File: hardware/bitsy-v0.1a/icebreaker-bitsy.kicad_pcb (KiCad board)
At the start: 4 copper layers, 38.1 x 17.8 mm, 95 parts, among them J1 Conn_01x01, J10 Conn_01x01, J11 Conn_01x01, J12 Conn_01x01, J13 Conn_01x01, J14 Jumper, J15 Jumper, J16 Jumper, J17 Jumper, J18 Jumper, J19 Jumper, J2 Conn_01x01, J20 Conn_01x01, J21 Conn_01x01, J22 Conn_01x01, J23 Conn_01x01, J24 Conn_01x01, J25 Conn_01x01, J26 Conn_01x01, J27 Conn_01x01, J28 Conn_01x01, J29 Conn_01x01, J3 Conn_01x01, J30 Conn_01x01, J31 Conn_01x01, J32 Conn_01x01, J33 Conn_01x01, J34 Conn_01x01, J35 Conn_01x01, J36 Conn_01x01, J37 Conn_01x01, J38 Jumper, J4 Conn_01x01, J41 Conn_01x01, J42 Conn_01x01, J43 Conn_01x01, J44 Conn_01x01, J45 Conn_01x01, J46 Conn_01x01, J47 Conn_01x01, J48 Conn_01x01, J49 Conn_01x01, J5 Conn_01x01, J6 Conn_01x01, J7 Conn_01x01, J8 Conn_01x01, J9 Conn_01x01, P1 USB_OTG, SW1 TACT, U1 USBLC6-2, U2 3.3V, U3 1V2, U5 W25Q, U6 ICE5LP4K-SG48, X1 12MHz

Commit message: Added pinout information and updated schematic.
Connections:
- net /IOT_36b renamed /IOT_36B
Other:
- board text added: "+3.3V xx 15"
- board text added: "16 xx GND"
- board text added: "17 25 IOT_36B"
- board text added: "18 26 IOT_39A"
- board text added: "19 27 IOT_38B"
- board text added: "20 28 IOT_41A"
- board text added: "21 31 IOT_42B"
- board text added: "22 32 IOT_43A"
- board text added: "23 34 IOT_44B"
- board text added: "24 36 IOT_48B"
- board text added: "25 39 ~LED_RED"
- board text added: "26 40 ~LED_GRN"
- board text added: "27 41 ~LED_BLU"
- board text added: "28 xx +1.2V"
- board text added: "29 xx +3.3V"
- board text added: "30 xx +5V"
- board text added: "36 20 IOB_25B_G3"
- board text added: "37 xx SCK"
- board text added: "38 21 IOB_23B"
- board text added: "39 xx SS_B/CS"
- board text added: "40 23 IOT_37A"
- board text added: "CDONE xx 33"
- board text added: "CRESET xx 35"
- board text added: "FLASH_MISO/IO1 xx 14"
- board text added: "FLASH_MOSI/IO0 xx 31"
- board text added: "GND xx 01"
- board text added: "IOB_0A 46 04"
- board text added: "IOB_13B 06 10"
- board text added: "IOB_16A 09 11"
- board text added: "IOB_22A FLASH_~WP~/IO2 12 13"
- board text added: "IOB_24A FLASH_~HLD~/~RST~/IO3 13 12"
- board text added: "IOB_29B 19 34"
- board text added: "IOB_2A 47 05"
- board text added: "IOB_31B 18 32"
- board text added: "IOB_3B_G6 44 02"
- board text added: "IOB_4A 48 06"
- board text added: "IOB_5B 45 03"
- board text added: "IOB_6A 02 07"
- board text added: "IOB_8A 04 09"
- board text added: "IOB_9B 03 08"

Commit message: Fixed pin header 3d models.
We had some of the models doubled up or not fully disabled. Now the TH
pin headers are all using KiCad V5 3d model locations and are all
disabled.

This fixes #23
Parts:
- removed REF**: 1b2_Logo_SilkS_5mm, pkl_logos:1b2_Logo_SilkS_5mm
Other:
- board text removed: "1Bitsquared (C) 2018"

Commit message: Added more legend silkscreen to ears.
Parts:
- added REF**: 1b2_Logo_SilkS_5mm, pkl_logos:1b2_Logo_SilkS_5mm, B.Cu at (41.6, 47.4)
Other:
- board text added: "1Bitsquared (C) 2018"
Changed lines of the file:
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@@
   (general
     (thickness 1.6)
-    (drawings 160)
+    (drawings 161)
     (tracks 669)
     (zones 0)
-    (modules 94)
+    (modules 95)
     (nets 60)
   )
@@
     (add_net "Net-(P1-Pad4)")
     (add_net "Net-(R7-Pad2)")
+  )
+  (module pkl_logos:1b2_Logo_SilkS_5mm locked (layer B.Cu)
+    (at 41.628314 47.429988 90)
+    (fp_text reference REF** (at 0 -4 90) (layer B.Fab) hide
+      (effects (font (size 1 1) (thickness 0.15)) (justify mirror))
+    )
+    (fp_text value 1b2_Logo_SilkS_5mm (at 0 4 90) (layer B.Fab) hide
+      (effects (font (size 1 1) (thickness 0.15)) (justify mirror))
+    )
+    (fp_line (start -0.5 0.5) (end -0.5 2.5) (layer B.SilkS) (width 0.2))
+    (fp_line (start -0.5 2.5) (end -2.5 2.5) (layer B.SilkS) (width 0.2))
+    (fp_line (start -2.5 2.5) (end -2.5 0.5) (layer B.SilkS) (width 0.2))
+    (fp_line (start -2.5 0.5) (end -0.5 0.5) (layer B.SilkS) (width 0.2))
+    (fp_line (start -0.5 2.5) (end 0 2) (layer B.SilkS) (width 0.2))
+    (fp_line (start 0 2) (end 0 0) (layer B.SilkS) (width 0.2))
+    (fp_line (start 0 0) (end -0.5 0.5) (layer B.SilkS) (width 0.2))
+    (fp_line (start -2.5 0.5) (end -2 0) (layer B.SilkS) (width 0.2))
+    (fp_line (start -2 0) (end 0 0) (layer B.SilkS) (width 0.2))
+    (fp_line (start 2 2) (end 0.5 2) (layer B.SilkS) (width 0.2))
+    (fp_line (start 0.5 2) (end 0.5 -0.5) (layer B.SilkS) (width 0.2))
+    (fp_line (start 0.5 -0.5) (end -2 -0.5) (layer B.SilkS) (width 0.2))
+    (fp_line (start -2 -0.5) (end -2 -2) (layer B.SilkS) (width 0.2))
+    (fp_line (start -2 -2) (end 2 -2) (layer B.SilkS) (width 0.2))
+    (fp_line (start 2 -2) (end 2 2) (layer B.SilkS) (width 0.2))
+    (fp_line (start 2 2) (end 2.5 1.5) (layer B.SilkS) (width 0.2))
+    (fp_line (start 2.5 1.5) (end 2.5 -2.5) (layer B.SilkS) (width 0.2))
+    (fp_line (start 2.5 -2.5) (end 2 -2) (layer B.SilkS) (width 0.2))
+    (fp_line (start -2 -2) (end -1.5 -2.5) (layer B.SilkS) (width 0.2))
+    (fp_line (start -1.5 -2.5) (end 2.5 -2.5) (layer B.SilkS) (width 0.2))
   )
   (module pkl_jumpers:J_0603 (layer B.Cu)
@@
       (net 2 +3V3))
   )
+  (gr_text "1Bitsquared\n(C) 2018" (at 37.4 47.3 270) (layer B.SilkS)
+    (effects (font (size 1 1) (thickness 0.25)) (justify mirror))
+  )
   (gr_line (start 79.2 38.6) (end 79.2 47.5) (layer Cmts.User) (width 0.2))

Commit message: Replaced/added the null logo to the boards.
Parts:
- REF**: value 1b2_Logo_SilkS_5mm -> null_Logo_SilkS_5mm; footprint pkl_logos:1b2_Logo_SilkS_5mm -> pkl_logos:null_Logo_SilkS_5mm
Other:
- board text added: "NULL"
- board text removed: "1Bitsquared (C) 2018"
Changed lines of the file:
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@@
-(kicad_pcb (version 20171130) (host pcbnew 5.1.2-f72e74a~84~ubuntu18.04.1)
+(kicad_pcb (version 20171130) (host pcbnew 5.1.5-52549c5~86~ubuntu19.10.1)
   (general
     (thickness 1.6)
@@
     (add_net "Net-(R7-Pad2)")
   )
-  (module pkl_logos:1b2_Logo_SilkS_5mm locked (layer B.Cu)
+  (module pkl_logos:null_Logo_SilkS_5mm locked (layer B.Cu)
     (at 41.628314 47.429988 90)
     (fp_text reference REF** (at 0 -4 90) (layer B.Fab) hide
       (effects (font (size 1 1) (thickness 0.15)) (justify mirror))
     )
-    (fp_text value 1b2_Logo_SilkS_5mm (at 0 4 90) (layer B.Fab) hide
+    (fp_text value null_Logo_SilkS_5mm (at 0 4 90) (layer B.Fab) hide
       (effects (font (size 1 1) (thickness 0.15)) (justify mirror))
     )
-    (fp_line (start -0.5 0.5) (end -0.5 2.5) (layer B.SilkS) (width 0.2))
-    (fp_line (start -0.5 2.5) (end -2.5 2.5) (layer B.SilkS) (width 0.2))
-    (fp_line (start -2.5 2.5) (end -2.5 0.5) (layer B.SilkS) (width 0.2))
-    (fp_line (start -2.5 0.5) (end -0.5 0.5) (layer B.SilkS) (width 0.2))
-    (fp_line (start -0.5 2.5) (end 0 2) (layer B.SilkS) (width 0.2))
-    (fp_line (start 0 2) (end 0 0) (layer B.SilkS) (width 0.2))
-    (fp_line (start 0 0) (end -0.5 0.5) (layer B.SilkS) (width 0.2))
-    (fp_line (start -2.5 0.5) (end -2 0) (layer B.SilkS) (width 0.2))
-    (fp_line (start -2 0) (end 0 0) (layer B.SilkS) (width 0.2))
-    (fp_line (start 2 2) (end 0.5 2) (layer B.SilkS) (width 0.2))
-    (fp_line (start 0.5 2) (end 0.5 -0.5) (layer B.SilkS) (width 0.2))
-    (fp_line (start 0.5 -0.5) (end -2 -0.5) (layer B.SilkS) (width 0.2))
-    (fp_line (start -2 -0.5) (end -2 -2) (layer B.SilkS) (width 0.2))
-    (fp_line (start -2 -2) (end 2 -2) (layer B.SilkS) (width 0.2))
-    (fp_line (start 2 -2) (end 2 2) (layer B.SilkS) (width 0.2))
-    (fp_line (start 2 2) (end 2.5 1.5) (layer B.SilkS) (width 0.2))
-    (fp_line (start 2.5 1.5) (end 2.5 -2.5) (layer B.SilkS) (width 0.2))
-    (fp_line (start 2.5 -2.5) (end 2 -2) (layer B.SilkS) (width 0.2))
-    (fp_line (start -2 -2) (end -1.5 -2.5) (layer B.SilkS) (width 0.2))
-    (fp_line (start -1.5 -2.5) (end 2.5 -2.5) (layer B.SilkS) (width 0.2))
+    (fp_arc (start -0.4 -0.2) (end -0.7 -0.2) (angle 180) (layer B.SilkS) (width 0.15))
+    (fp_line (start 1 -0.5) (end 1.5 -0.5) (layer B.SilkS) (width 0.15))
+    (fp_line (start 1 0.5) (end 1 -0.5) (layer B.SilkS) (width 0.15))
+    (fp_line (start 0.2 -0.5) (end 0.7 -0.5) (layer B.SilkS) (width 0.15))
+    (fp_line (start 0.2 0.5) (end 0.2 -0.5) (layer B.SilkS) (width 0.15))
+    (fp_line (start -0.1 0.5) (end -0.1 -0.2) (layer B.SilkS) (width 0.15))
+    (fp_line (start -0.7 0.5) (end -0.7 -0.2) (layer B.SilkS) (width 0.15))
+    (fp_line (start -1 -0.5) (end -1 0.5) (layer B.SilkS) (width 0.15))
+    (fp_line (start -1.5 0.5) (end -1 -0.5) (layer B.SilkS) (width 0.15))
+    (fp_line (start -1.5 -0.5) (end -1.5 0.5) (layer B.SilkS) (width 0.15))
+    (fp_line (start 2.5 2.5) (end -2.5 2.5) (layer B.SilkS) (width 0.2))
+    (fp_line (start -2.5 2.5) (end -2.5 -2.5) (layer B.SilkS) (width 0.2))
+    (fp_line (start 2.5 2.5) (end 2.5 -2.5) (layer B.SilkS) (width 0.2))
+    (fp_line (start -2.5 -2.5) (end 2.5 -2.5) (layer B.SilkS) (width 0.2))
   )
   (module pkl_jumpers:J_0603 (layer B.Cu)
@@
       (net 2 +3V3))
   )
-  (gr_text "1Bitsquared\n(C) 2018" (at 37.4 47.3 270) (layer B.SilkS)
+  (gr_text NULL (at 37.4 47.3 270) (layer B.SilkS)
     (effects (font (size 1 1) (thickness 0.25)) (justify mirror))
   )

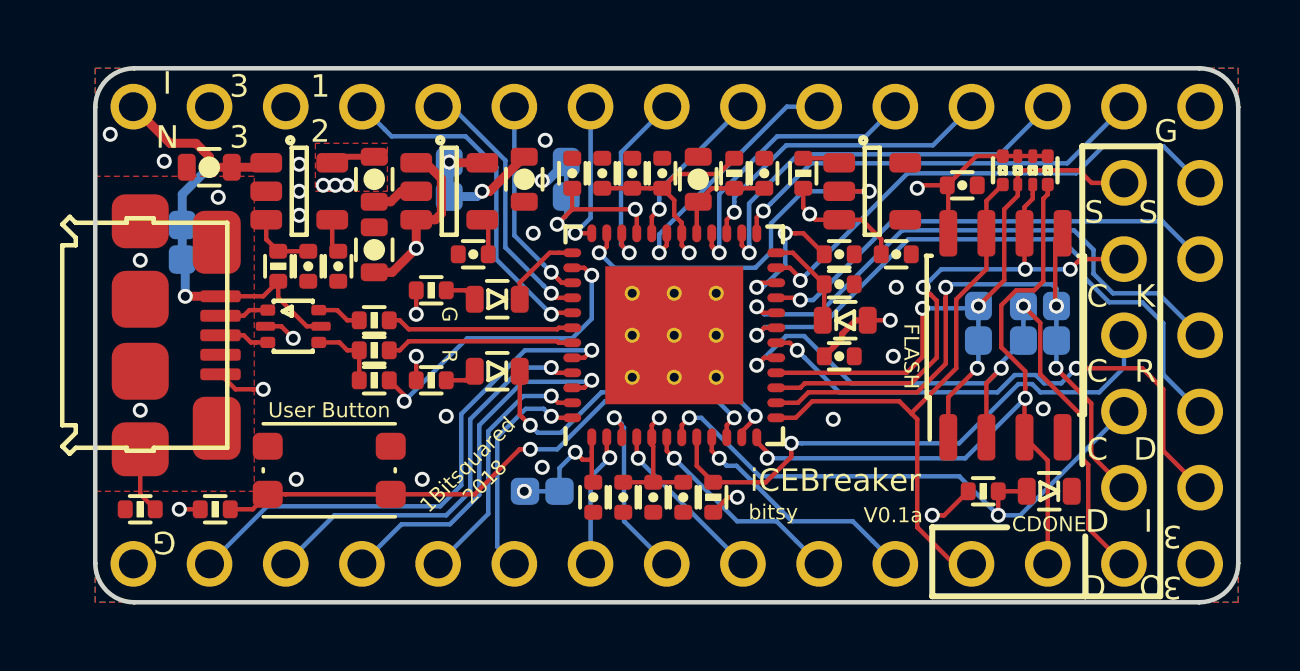
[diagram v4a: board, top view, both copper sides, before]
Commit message: Updated all design files to KiCad V8.0.6.
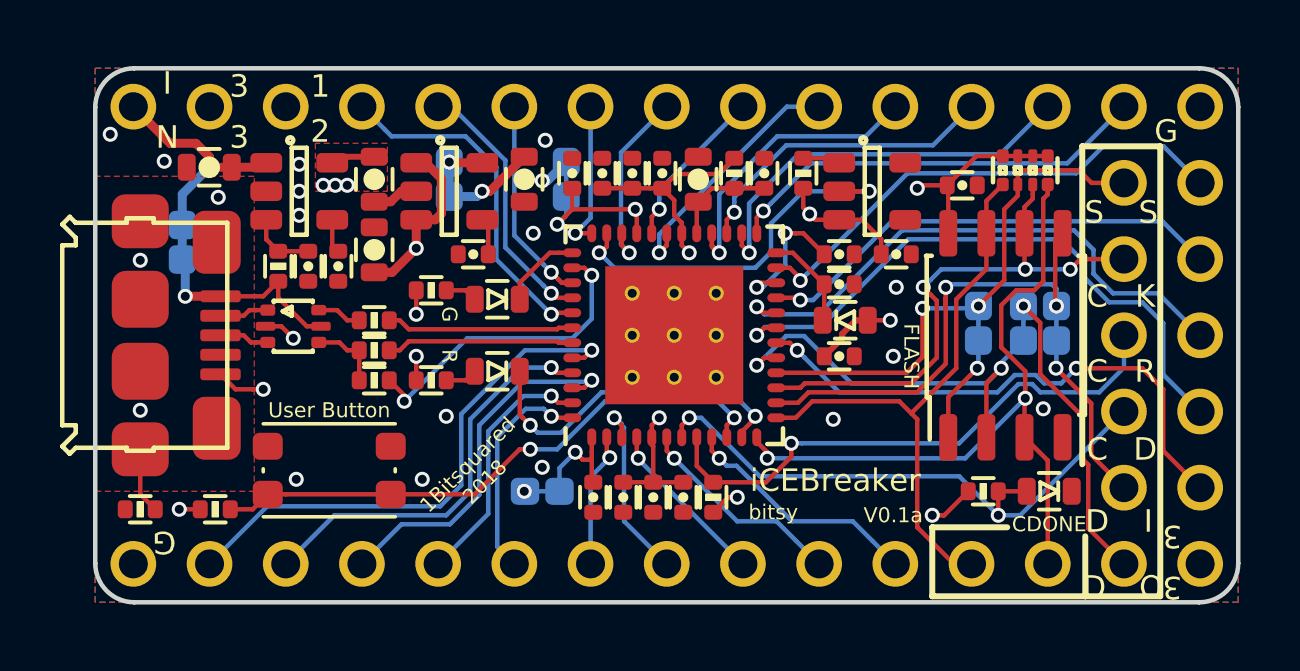
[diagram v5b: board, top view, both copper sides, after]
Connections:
- net /FLASH_~HLD~/~RST~/IO3 renamed /FLASH_~{HLD}/~{RST}/IO3
- net /FLASH_~WP~/IO2 renamed /FLASH_~{WP}/IO2
- net /~BUTTON renamed /~{BUTTON}
- net /~LEDG renamed /~{LEDG}
- net /~LEDR renamed /~{LEDR}
- net /~LED_BLU renamed /~{LED_BLU}
- net /~LED_GRN renamed /~{LED_GRN}
- net /~LED_RED renamed /~{LED_RED}
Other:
- net class Default removed
- board text added: "25 39 ~{LED_RED}"
- board text added: "26 40 ~{LED_GRN}"
- board text added: "27 41 ~{LED_BLU}"
- board text added: "IOB_22A FLASH_~{WP}/IO2 12 13"
- board text added: "IOB_24A FLASH_~{HLD}/~{RST}/IO3 13 12"
- board text removed: "25 39 ~LED_RED"
- board text removed: "26 40 ~LED_GRN"
- board text removed: "27 41 ~LED_BLU"
- board text removed: "IOB_22A FLASH_~WP~/IO2 12 13"
- board text removed: "IOB_24A FLASH_~HLD~/~RST~/IO3 13 12"
